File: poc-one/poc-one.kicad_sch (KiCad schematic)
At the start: 44 parts, among them J2 Conn_02x26_Odd_Even, J3 Conn_02x26_Odd_Even, J4 Connector, USB-TYPE-C-16P, SW1 SW_Push, SW2 SW_Push, U1 RP2350_80QFN, U2 NCP1117-3.3_SOT223, U3 W25Q128, Y1 ABM8-272-T3

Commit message: schematic-v2
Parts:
- removed C1, C5: 10u, Capacitor_SMD:C_0805_2012Metric, symbol Device:C
- removed H1, H2, H3, H4: MountingHole, MountingHole:MountingHole_2.7mm_M2.5, symbol Mechanical:MountingHole
- removed J2, J3: Conn_02x26_Odd_Even, Connector_PinHeader_2.54mm:PinHeader_2x26_P2.54mm_Vertical, symbol Connector_Generic:Conn_02x26_Odd_Even
- removed J4: Connector, USB-TYPE-C-16P, PCM_JLCPCB:TYPE-C-SMD_HX-TYPE-C-16PIN, symbol PCM_JLCPCB-Extended:Connector, USB-TYPE-C-16P
- removed R5, R9: 5.1k, Resistor_SMD:R_0402_1005Metric, symbol Device:R
- removed U2: NCP1117-3.3_SOT223, Package_TO_SOT_SMD:SOT-223-3_TabPin2, symbol Regulator_Linear:NCP1117-3.3_SOT223
- added J1, J5, J6: Conn_02x10_Odd_Even, symbol Connector_Generic:Conn_02x10_Odd_Even
- added JP1, JP10, JP11, JP12, JP13, JP14, JP15, JP16, JP17, JP18, JP19, JP2, JP20, JP21, JP3, JP4, JP5, JP6, JP7, JP8, JP9: SolderJumper_2_Bridged, Jumper:SolderJumper-2_P1.3mm_Bridged_Pad1.0x1.5mm, symbol Jumper:SolderJumper_2_Bridged
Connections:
- net +3V3: now also J1.1 (Pin_1), J1.19 (Pin_19), J1.2 (Pin_2), J1.20 (Pin_20), J5.1 (Pin_1), J5.19 (Pin_19), J5.2 (Pin_2), J5.20 (Pin_20), J6.1 (Pin_1), J6.19 (Pin_19), J6.2 (Pin_2), J6.20 (Pin_20)
- net GND: now also J1.11 (Pin_11), J1.13 (Pin_13), J1.15 (Pin_15), J1.17 (Pin_17), J1.3 (Pin_3), J1.5 (Pin_5), J1.7 (Pin_7), J1.9 (Pin_9), J5.11 (Pin_11), J5.13 (Pin_13), J5.15 (Pin_15), J5.17 (Pin_17), J5.3 (Pin_3), J5.5 (Pin_5), J5.7 (Pin_7), J5.9 (Pin_9), J6.11 (Pin_11), J6.13 (Pin_13), J6.15 (Pin_15), J6.17 (Pin_17), J6.3 (Pin_3), J6.5 (Pin_5), J6.7 (Pin_7), J6.9 (Pin_9)
- net GPIO10: now also J5.6 (Pin_6)
- net GPIO11: now also J5.8 (Pin_8)
- net GPIO12: now also J5.10 (Pin_10)
- net GPIO13: now also J5.12 (Pin_12)
- net GPIO14: now also J5.14 (Pin_14)
- net GPIO15: now also J5.16 (Pin_16)
- net GPIO16: now also J5.18 (Pin_18)
- net GPIO7: now also J5.4 (Pin_4)
- net SWCLK: now also J6.18 (Pin_18)
- net SWD: now also J6.16 (Pin_16)
- net GPIO0 renamed M-RX
- net M-RX: now also J6.4 (Pin_4)
- net GPIO1 renamed M-TX
- net M-TX: now also J6.6 (Pin_6)
- net GPIO17: no longer names the net of U1.17 (GPIO17)
- net GPIO17: now also JP1.1 (A)
- net GPIO18: no longer names the net of U1.18 (GPIO18)
- net GPIO18: now also JP2.1 (A)
- net GPIO19: no longer names the net of U1.19 (GPIO19)
- net GPIO19: now also JP3.1 (A)
- net GPIO2 renamed M-SCK
- net M-SCK: now also J6.8 (Pin_8)
- net GPIO20: no longer names the net of U1.20 (GPIO20)
- net GPIO20: now also JP4.1 (A)
- net GPIO21: no longer names the net of U1.21 (GPIO21)
- net GPIO21: now also JP5.1 (A)
- net GPIO22: no longer names the net of U1.22 (GPIO22)
- net GPIO22: now also JP6.1 (A)
- net GPIO23: no longer names the net of U1.23 (GPIO23)
- net GPIO23: now also JP7.1 (A)
- net GPIO24: no longer names the net of U1.25 (GPIO24)
- net GPIO24: now also JP8.1 (A)
- net GPIO25: no longer names the net of U1.26 (GPIO25)
- net GPIO25: now also JP9.1 (A)
- net GPIO26: no longer names the net of U1.27 (GPIO26)
- net GPIO26: now also JP10.1 (A)
- net GPIO27: no longer names the net of U1.28 (GPIO27)
- net GPIO27: now also JP11.1 (A)
- net GPIO28: no longer names the net of U1.36 (GPIO28)
- net GPIO28: now also JP12.1 (A)
- net GPIO29: no longer names the net of U1.37 (GPIO29)
- net GPIO29: now also JP13.1 (A)
- net GPIO3 renamed M-COPI
- net M-COPI: now also J6.10 (Pin_10)
- net GPIO30: no longer names the net of U1.38 (GPIO30)
- net GPIO30: now also JP14.1 (A)
- net GPIO31: no longer names the net of U1.39 (GPIO31)
- net GPIO31: now also JP15.1 (A)
- net GPIO32: no longer names the net of U1.40 (GPIO32)
- net GPIO32: now also JP16.1 (A)
- net GPIO33: no longer names the net of U1.42 (GPIO33)
- net GPIO33: now also JP17.1 (A)
- net GPIO34: no longer names the net of U1.43 (GPIO34)
- net GPIO34: now also JP18.1 (A)
- net GPIO35: no longer names the net of U1.44 (GPIO35)
- net GPIO35: now also JP19.1 (A)
- net GPIO36: no longer names the net of U1.45 (GPIO36)
- net GPIO36: now also JP20.1 (A)
- net GPIO37: no longer names the net of U1.46 (GPIO37)
- net GPIO37: now also JP21.1 (A)
- net GPIO38: no longer names the net of U1.47 (GPIO38)
- net GPIO39: no longer names the net of U1.48 (GPIO39)
- net GPIO4 renamed M-CIPO
- net M-CIPO: now also J6.12 (Pin_12)
- net GPIO40_ADC0 renamed TOUCH1
- net TOUCH1: now also J1.4 (Pin_4)
- net GPIO41_ADC1 renamed TOUCH2
- net TOUCH2: now also J1.6 (Pin_6)
- net GPIO42_ADC2 renamed TOUCH3
- net TOUCH3: now also J1.8 (Pin_8)
- net GPIO43_ADC3 renamed TOUCH4
- net TOUCH4: now also J1.10 (Pin_10)
- net GPIO44_ADC4 renamed TOUCH5
- net TOUCH5: now also J1.12 (Pin_12)
- net GPIO45_ADC5 renamed TOUCH6
- net TOUCH6: now also J1.14 (Pin_14)
- net GPIO46_ADC6 renamed TOUCH7
- net TOUCH7: now also J1.16 (Pin_16)
- net GPIO47_ADC7 renamed TOUCH8
- net TOUCH8: now also J1.18 (Pin_18)
- net GPIO5 renamed M-CS
- net M-CS: now also J6.14 (Pin_14)
- net GPIO6 renamed Battery/INT
- net GPIO8 renamed Battery/SDA
- net GPIO9 renamed Battery/SCL
- net RUN renamed RESET
- net USB_D+ renamed Battery/USB_D+
- net USB_D- renamed Battery/USB_D-
- net VREG_AVDD: no longer names the net of C9.1, R3.2, U1.61 (VREG_AVDD)
- net VREG_LX: no longer names the net of L1.2, U1.63 (VREG_LX)
- net XIN: no longer names the net of C3.1, U1.30 (XIN), Y1.1
- net XOUT: no longer names the net of R2.1, U1.31 (XOUT)
- net ~{USB_BOOT} renamed BOOTSEL
- new net LED_control/CLK: JP2.2 (B)
- new net LED_control/C_P_1: JP4.2 (B)
- new net LED_control/C_P_2: JP5.2 (B)
- new net LED_control/C_P_3: JP6.2 (B)
- new net LED_control/C_P_4: JP7.2 (B)
- new net LED_control/C_P_5: JP8.2 (B)
- new net LED_control/C_P_6: JP9.2 (B)
- new net LED_control/R_S_1_B: JP18.2 (B)
- new net LED_control/R_S_1_G: JP14.2 (B)
- new net LED_control/R_S_1_R: JP10.2 (B)
- new net LED_control/R_S_2_B: JP19.2 (B)
- new net LED_control/R_S_2_G: JP15.2 (B)
- new net LED_control/R_S_2_R: JP11.2 (B)
- new net LED_control/R_S_3_B: JP20.2 (B)
- new net LED_control/R_S_3_G: JP16.2 (B)
- new net LED_control/R_S_3_R: JP12.2 (B)
- new net LED_control/R_S_4_B: JP21.2 (B)
- new net LED_control/R_S_4_G: JP17.2 (B)
- new net LED_control/R_S_4_R: JP13.2 (B)
- new net LED_control/STOP: JP3.2 (B)
- new net LED_control/~{OE}: JP1.2 (B)
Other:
- added sheet Battery (battery.kicad_sch)
- sheet LED_control: file untitled.kicad_sch -> led_control.kicad_sch
- note added: "0-1 UART-0 to master (crossed over here)"
- note added: "2-5 SPI-0 to master"
- note added: "40-47 reserved for touch inputs here broken out"
- note added: "8-9 I2C-0 for battery"
- note added: "reserved"
- note removed: "Power"
- moved on the sheet: C2, C3, C4, R1, R10, R2, R4, R7, R8, SW2, U3

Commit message: poc-one update & bom
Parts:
- removed J1: Conn_02x10_Odd_Even, symbol Connector_Generic:Conn_02x10_Odd_Even
- J5: value Conn_02x10_Odd_Even -> SUBG_FANOUT; footprint (none) -> Connector_PinHeader_2.54mm:PinHeader_2x10_P2.54mm_Vertical
- J6: value Conn_02x10_Odd_Even -> MASTER_FANOUT; footprint (none) -> Connector_PinHeader_2.54mm:PinHeader_2x10_P2.54mm_Vertical
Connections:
- net GND: now also C20.1; no longer C20.2
- net GPIO7: no longer J5.4 (Pin_4)
- net +3V3 renamed +3.3VADC
- net +3.3VADC: now also C20.2; no longer C20.1
- net GPIO10 renamed SUBG_COPI
- net SUBG_COPI: now also U1.9 (GPIO11); no longer U1.8 (GPIO10)
- net GPIO11 renamed SUBG_CIPO
- net SUBG_CIPO: now also U1.11 (GPIO12); no longer U1.9 (GPIO11)
- net GPIO12 renamed SUBG_CS
- net SUBG_CS: now also U1.12 (GPIO13); no longer U1.11 (GPIO12)
- net GPIO13 renamed GPIO_7
- net GPIO_7: no longer U1.12 (GPIO13)
- net TOUCH1 renamed Analog/MIC_OUT
- net TOUCH2 renamed Analog/AMB_LIGHT_OUT
- net TOUCH3 renamed Analog/TOUCH1
- net TOUCH4 renamed Analog/TOUCH2
- net TOUCH5 renamed Analog/TOUCH3
- net TOUCH6 renamed Analog/TOUCH4
- net TOUCH7 renamed Analog/TOUCH5
- net TOUCH8 renamed Analog/TOUCH6
- new net SUBG_SCK: J5.4 (Pin_4), U1.8 (GPIO10)
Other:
- added sheet Analog (analog.kicad_sch)
- note added: "10-13 SPI-1 to Sub-G receiver 7,14,15,16 reserved for SubG"
- note added: "WISHLIST: - NFC - that badge connector -> doesn't make sense, too large for this board - sub ghz receiver"
- note added: "reserved for LED"
- note added: "todo: accurate shunt of adc_avdd to 3.00v using shunt (e.g. lm4040) refer to rp zero 2 for schematic"
- note added: "todo: push button footprint C6467298"
- note removed: "40-47 reserved for touch inputs here broken out"
- note removed: "reserved"
- moved on the sheet: C21

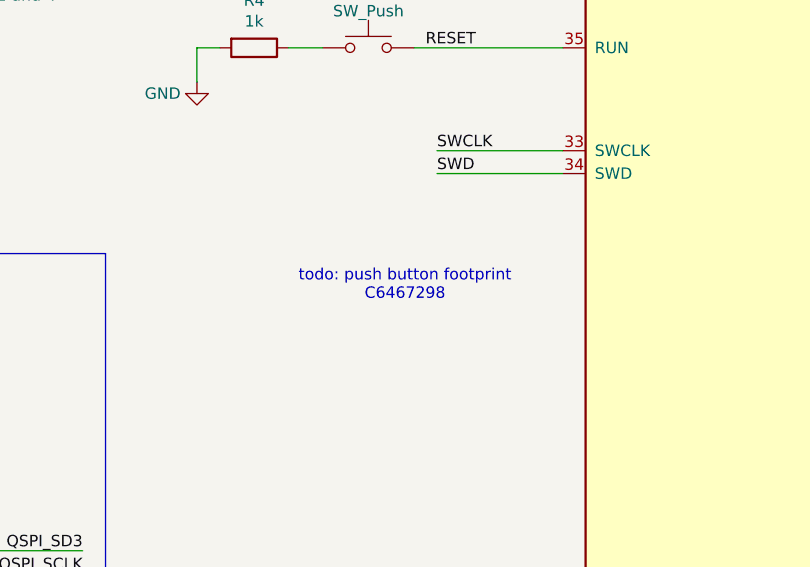
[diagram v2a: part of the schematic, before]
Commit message: fixed a couple resistors, reworked footprints incl. datasheets
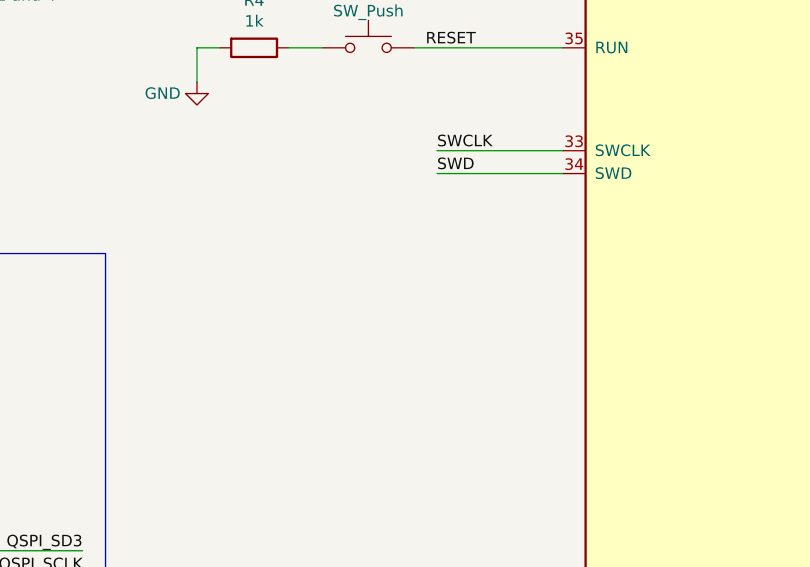
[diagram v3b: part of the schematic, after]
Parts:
- J5, J6: now left out of the parts list
- SW1, SW2: footprint Button_Switch_SMD:SW_Push_1P1T_NO_Vertical_Wuerth_434133025816 -> TFPC:B3U-1100PM
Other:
- note removed: "todo: push button footprint C6467298"
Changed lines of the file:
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@@
 		)
 	)
-	(text "todo: push button footprint\nC6467298"
-		(exclude_from_sim no)
-		(at 151.384 194.056 0)
-		(effects
-			(font
-				(size 1.27 1.27)
-			)
-		)
-	)
 	(text "WISHLIST:\n- NFC\n- that badge connector -> doesn't make sense, too large for this board\n- sub ghz receiver"
 		(exclude_from_sim no)
@@
 			)
 		)
-		(property "Footprint" "Button_Switch_SMD:SW_Push_1P1T_NO_Vertical_Wuerth_434133025816"
+		(property "Footprint" "TFPC:B3U-1100PM"
 			(at 147.32 162.56 0)
 			(hide yes)
@@
 		(body_style 1)
 		(exclude_from_sim no)
-		(in_bom yes)
+		(in_bom no)
 		(on_board yes)
-		(in_pos_files yes)
+		(in_pos_files no)
 		(dnp no)
 		(fields_autoplaced yes)
@@
 		(body_style 1)
 		(exclude_from_sim no)
-		(in_bom yes)
+		(in_bom no)
 		(on_board yes)
-		(in_pos_files yes)
+		(in_pos_files no)
 		(dnp no)
 		(fields_autoplaced yes)
@@
 			)
 		)
-		(property "Footprint" "Button_Switch_SMD:SW_Push_1P1T_NO_Vertical_Wuerth_434133025816"
+		(property "Footprint" "TFPC:B3U-1100PM"
 			(at 127 133.35 0)
 			(hide yes)

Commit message: poc-one routed & schematic changes
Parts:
- removed C2: 100n, Capacitor_SMD:C_0402_1005Metric, symbol Device:C
- removed R10: 0, Resistor_SMD:R_0402_1005Metric, symbol Device:R
- removed U3: W25Q128, PCM_JLCPCB:SOIC-8_L5.3-W5.3-P1.27-LS8.0-BL, symbol PCM_JLCPCB-Memory:16MByte, SPI
- added C39: 100n, Capacitor_SMD:C_0402_1005Metric, symbol Device:C
- added J5: DEBUG, Connector_PinHeader_2.54mm:PinHeader_1x03_P2.54mm_Vertical, symbol Connector:Conn_01x03_Pin
- JP1, JP10, JP11, JP12, JP13, JP14, JP15, JP16, JP17, JP18, JP19, JP2, JP20, JP21, JP3, JP4, JP5, JP6, JP7, JP8, JP9: now in the parts list
- R1: value DNF -> 0; footprint Resistor_SMD:R_0402_1005Metric -> PCM_JLCPCB:R_0603
- U2: renamed from U1; value RP2350_80QFN -> RP2354_80QFN
- renumbered C3 to C1, C12 to C10, C20 to C11, C13 to C12, C14 to C13, C15 to C14, C16 to C15, C17 to C16, C18 to C17, C21 to C18, C4 to C2, C6 to C4, C7 to C5, C8 to C6, C9 to C7, C10 to C8, C11 to C9, J6 to J1, J5 to J2, R2 to R3, R3 to R5
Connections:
- net FLASH_SS is gone; now on net +3.3VADC: R1.2
- net GPIO7 is gone; now on net Battery/SCL: U2.4 (GPIO7)
- net GPIO_7 is gone; now on net SUBG_CS: J2.12 (Pin_12)
- net +3.3VADC: no longer C10.1, C12.1, C13.1, C14.1, C15.1, C16.1, C17.1, C18.1, C4.1, J1.1 (Pin_1), J1.19 (Pin_19), J1.2 (Pin_2), J1.20 (Pin_20), J2.1 (Pin_1), J2.19 (Pin_19), J2.2 (Pin_2), J2.20 (Pin_20), R1.1, R5.1, U2.15 (IOVDD), U2.24 (IOVDD), U2.29 (IOVDD), U2.41 (IOVDD), U2.5 (IOVDD), U2.50 (IOVDD), U2.60 (IOVDD), U2.64 (VREG_VIN), U2.68 (USB_OTP_VDD), U2.69 (QSPI_IOVDD), U2.76 (IOVDD)
- net Analog/AMB_LIGHT_OUT: now also U2.49 (GPIO40_ADC0); no longer U2.52 (GPIO41_ADC1)
- net Analog/MIC_OUT: now also U2.58 (GPIO47_ADC7); no longer U2.49 (GPIO40_ADC0)
- net Analog/TOUCH1: now also U2.52 (GPIO41_ADC1); no longer U2.53 (GPIO42_ADC2)
- net Analog/TOUCH2: now also U2.53 (GPIO42_ADC2); no longer U2.54 (GPIO43_ADC3)
- net Analog/TOUCH3: now also U2.54 (GPIO43_ADC3); no longer U2.55 (GPIO44_ADC4)
- net Analog/TOUCH4: now also U2.55 (GPIO44_ADC4); no longer U2.56 (GPIO45_ADC5)
- net Analog/TOUCH5: now also U2.56 (GPIO45_ADC5); no longer U2.57 (GPIO46_ADC6)
- net Analog/TOUCH6: now also U2.57 (GPIO46_ADC6); no longer U2.58 (GPIO47_ADC7)
- net BOOTSEL: now also U2.75 (QSPI_SS); no longer R6.2
- net Battery/INT: now also U2.6 (GPIO8); no longer U2.3 (GPIO6)
- net Battery/SCL: no longer U2.7 (GPIO9)
- net Battery/SDA: now also U2.3 (GPIO6); no longer U2.6 (GPIO8)
- net GND: now also J1.16 (Pin_16), J1.18 (Pin_18), R6.2, C39.2, J5.1 (Pin_1); no longer SW1.1
- net SUBG_CIPO: now also J2.10 (Pin_10); no longer J2.8 (Pin_8)
- net SUBG_COPI: now also J2.8 (Pin_8); no longer J2.6 (Pin_6)
- net SUBG_CS: no longer J2.10 (Pin_10)
- net SUBG_SCK: now also J2.6 (Pin_6); no longer J2.4 (Pin_4)
- net QSPI_SCLK: no longer names the net of U2.71 (QSPI_SCLK)
- net QSPI_SD0: no longer names the net of U2.72 (QSPI_SD0)
- net QSPI_SD1: no longer names the net of U2.74 (QSPI_SD1)
- net QSPI_SD2: no longer names the net of U2.73 (QSPI_SD2)
- net QSPI_SD3: no longer names the net of U2.70 (QSPI_SD3)
- net QSPI_SS: no longer names the net of R6.1
- net QSPI_SS: now also SW1.1; no longer U2.75 (QSPI_SS)
- net SWCLK: no longer names the net of U2.33 (SWCLK)
- net SWCLK: now also J5.2 (Pin_2); no longer J1.18 (Pin_18)
- net SWD: no longer names the net of U2.34 (SWD)
- net SWD: now also J5.3 (Pin_3); no longer J1.16 (Pin_16)
- new net +3V3: C10.1, C12.1, C13.1, C14.1, C15.1, C16.1, C17.1, C18.1, C39.1, C4.1, J1.1 (Pin_1), J1.19 (Pin_19), J1.2 (Pin_2), J1.20 (Pin_20), J2.1 (Pin_1), J2.19 (Pin_19), J2.2 (Pin_2), J2.20 (Pin_20), R1.1, R5.1, U2.15 (IOVDD), U2.24 (IOVDD), U2.29 (IOVDD), U2.41 (IOVDD), U2.5 (IOVDD), U2.50 (IOVDD), U2.60 (IOVDD), U2.64 (VREG_VIN), U2.68 (USB_OTP_VDD), U2.69 (QSPI_IOVDD), U2.76 (IOVDD)
- new net GPIO9: J2.4 (Pin_4), U2.7 (GPIO9)
- no-connect marks 2 -> 7
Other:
- note added: "10-13 SPI-1 to Sub-G receiver 9,14,15,16 reserved for SubG"
- note added: "6-7 I2C-1 for battery 8 battery interrupt"
- note added: "TODO ASSEMBLY: - battery 90 deg left rotate - u6 90 deg right rotate - q1-q6 180 deg rotate - leds 180 deg rotate - SW1 / SW2 180 deg rotate -- fix offset - l1 rotate 180 deg - u4 rotate 180 deg - sw3 90 deg right - u3 90 deg right - c27 who fucking knows there is no 3d model"
- note added: "TODO: silkscreen"
- note added: "warning: manually adjusted pad clearance for C4/C5 to 0.12mm to leave enough space for a wide VREG_LX. Theoretically 0.15mm spacing and 0.1mm trace would work. TODO: check with JLC whether 0.12mm / 0.16mm work or if 0.15mm / 0.1mm is better (and pray that it doesn't fuck up power)"
- note removed: "10-13 SPI-1 to Sub-G receiver 7,14,15,16 reserved for SubG"
- note removed: "8-9 I2C-0 for battery"
- note removed: "Primary Flash"
- note removed: "omit if using rp2354"
- note removed: "other flash probably needs R1 10k, in that case DNF R10"
- moved on the sheet: R6, SW1
